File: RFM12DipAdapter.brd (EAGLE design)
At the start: 25 x 22 mm, 5 parts

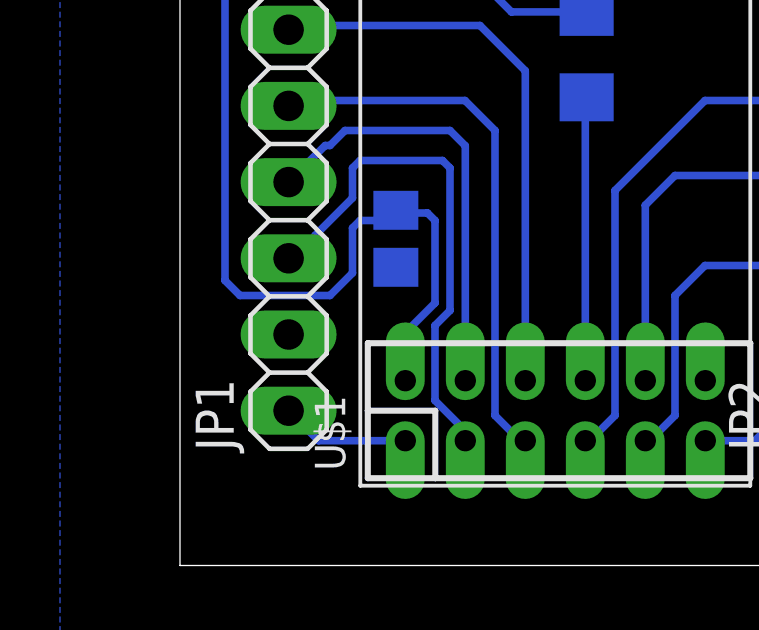
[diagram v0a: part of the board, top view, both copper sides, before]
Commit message: Forgot VCC line
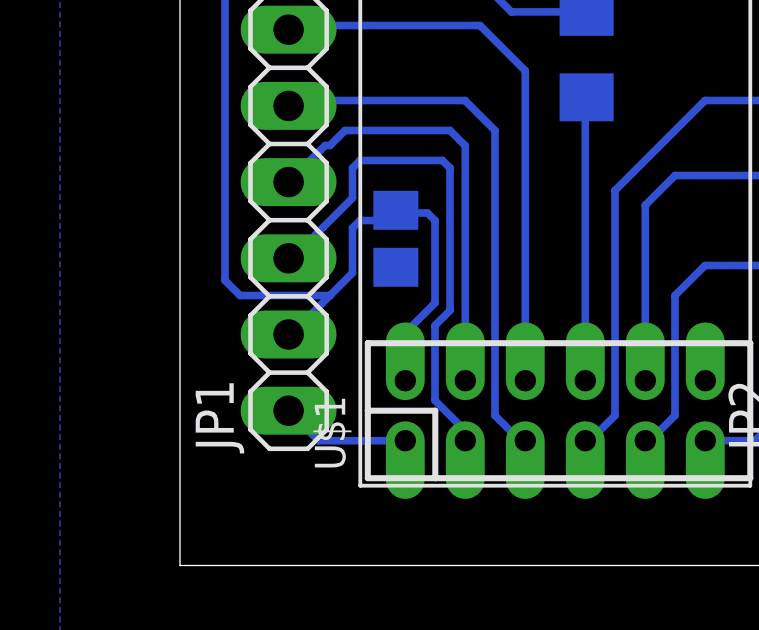
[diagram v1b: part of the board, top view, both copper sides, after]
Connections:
- removed net VDD: JP1.2
- net VCC: now also JP1.2
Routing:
- net VCC: track 37.3 -> 39.2 mm
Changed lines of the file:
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@@
 <wire x1="8.25" y1="10.75" x2="7.285" y2="10.75" width="0.254" layer="16"/>
 <wire x1="7.285" y1="10.75" x2="7.195" y2="10.84" width="0.254" layer="16"/>
+<contactref element="JP1" pad="2"/>
+<wire x1="3.62" y1="6.7" x2="3.7" y2="6.7" width="0.254" layer="16"/>
+<wire x1="3.7" y1="6.7" x2="5" y2="8" width="0.254" layer="16"/>
 </signal>
 <signal name="SEL">
@@
 <wire x1="4.62" y1="3.16" x2="3.62" y2="4.16" width="0.254" layer="16"/>
 </signal>
-<signal name="VDD">
-<contactref element="JP1" pad="2"/>
-</signal>
 <signal name="NC">
